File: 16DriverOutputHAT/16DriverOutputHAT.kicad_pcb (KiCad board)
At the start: 2 copper layers, 65 x 56 mm, 19 parts, among them J0 RPi_GPIO, P1 A7 A6 A5 A4 A3 A2 A1 A0 C, P2 C B0 B1 B2 B3 B4 B5 B6 B7, P3 0 1 2, U1 MCP23017, U2 TBD62X83A, U3 TBD62X83A

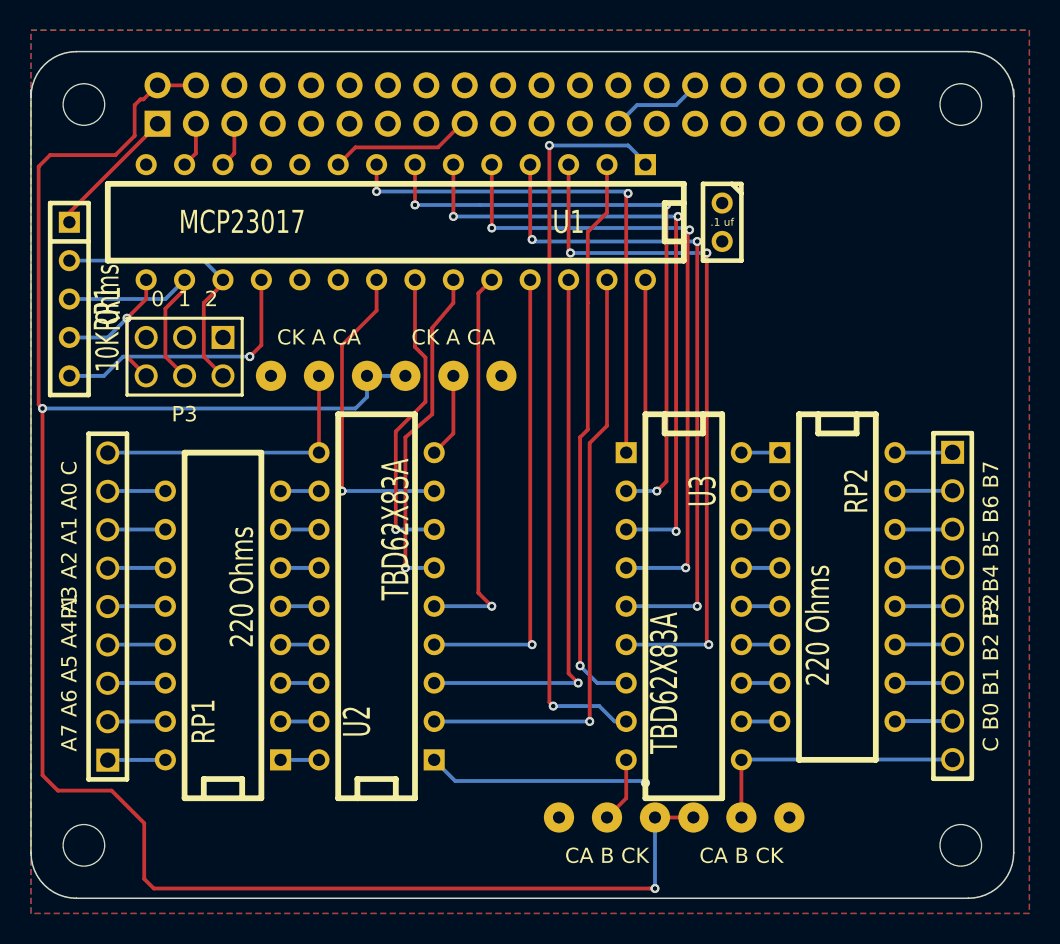
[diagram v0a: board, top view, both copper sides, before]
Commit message: Update 16DriverOutputHAT to user a 12V supply for the LEDs, adding a screw terminal for the 12 supply and changing the load resistors to 1.5K.
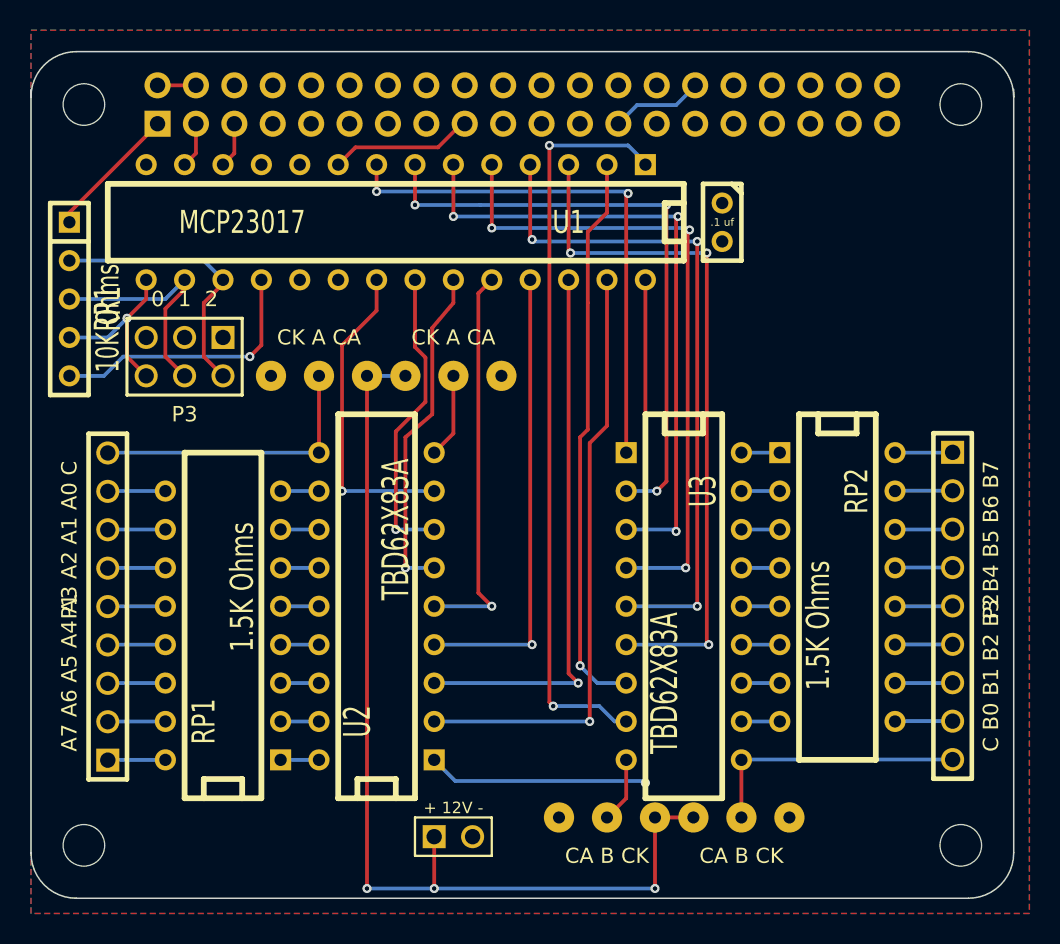
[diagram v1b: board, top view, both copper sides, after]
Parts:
- added T1: + 12V -, ScrewTerm2.54-2, F.Cu at (66.0, 83.8)
- RP1, RP2: value 220 Ohms -> 1.5K Ohms
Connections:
- JP1 pad 1: +5V -> +12V
- JP2 pad 3: +5V -> +12V
- JP3 pad 1: +5V -> +12V
- JP4 pad 3: +5V -> +12V
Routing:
- net +5V: track 132.9 -> 2.54 mm, vias 2 -> 0
- net +12V: track 0.00 -> 66.2 mm, vias 0 -> 3
